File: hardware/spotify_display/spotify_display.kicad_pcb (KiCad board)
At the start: 2 copper layers, 5 parts, among them SW1 SW_Push, SW2 SW_Push, SW3 SW_Push, U1 WEMOS_C3_mini, U2 ST7735

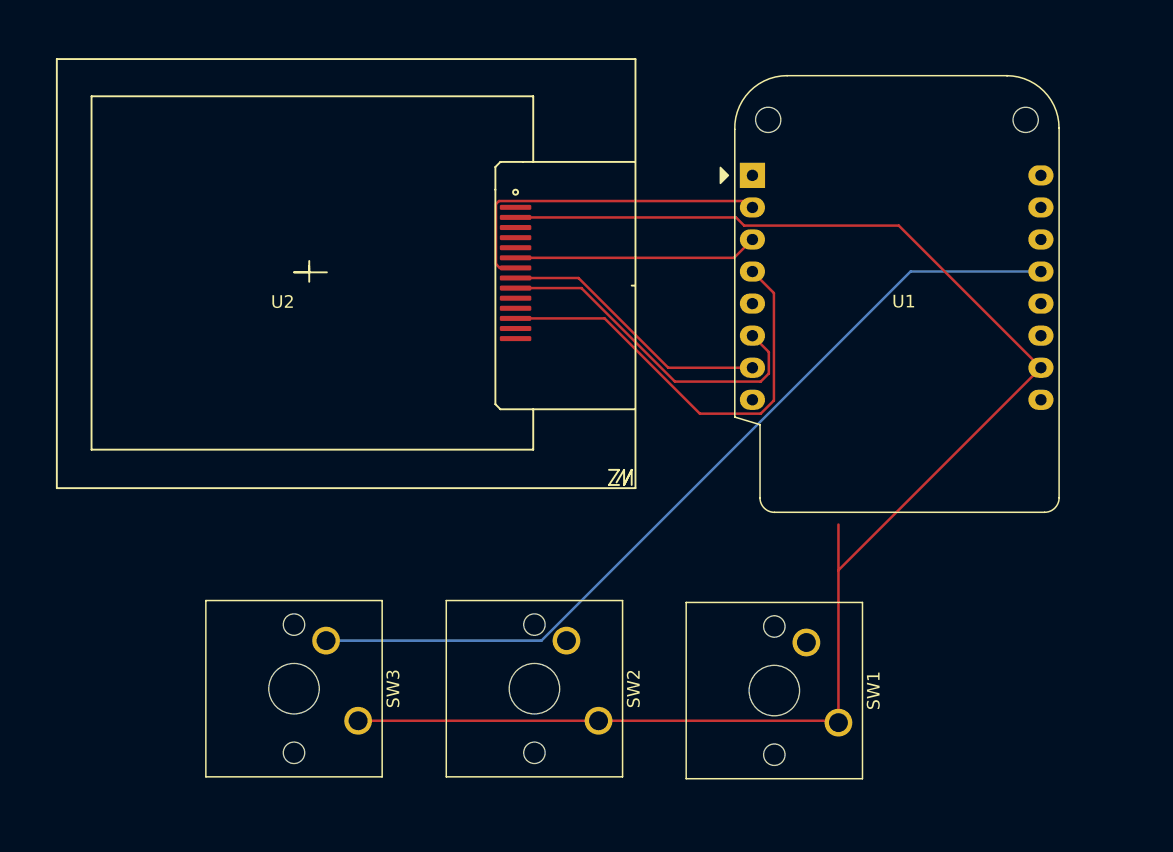
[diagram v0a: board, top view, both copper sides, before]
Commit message: Add Rotary Encoder component and update project files
- Added a new Rotary Encoder symbol to the schematic with properties including reference, value, footprint, and description.
- Updated the KiCad project configuration to specify the plot output directory.
- Adjusted column widths in the project settings for better layout.
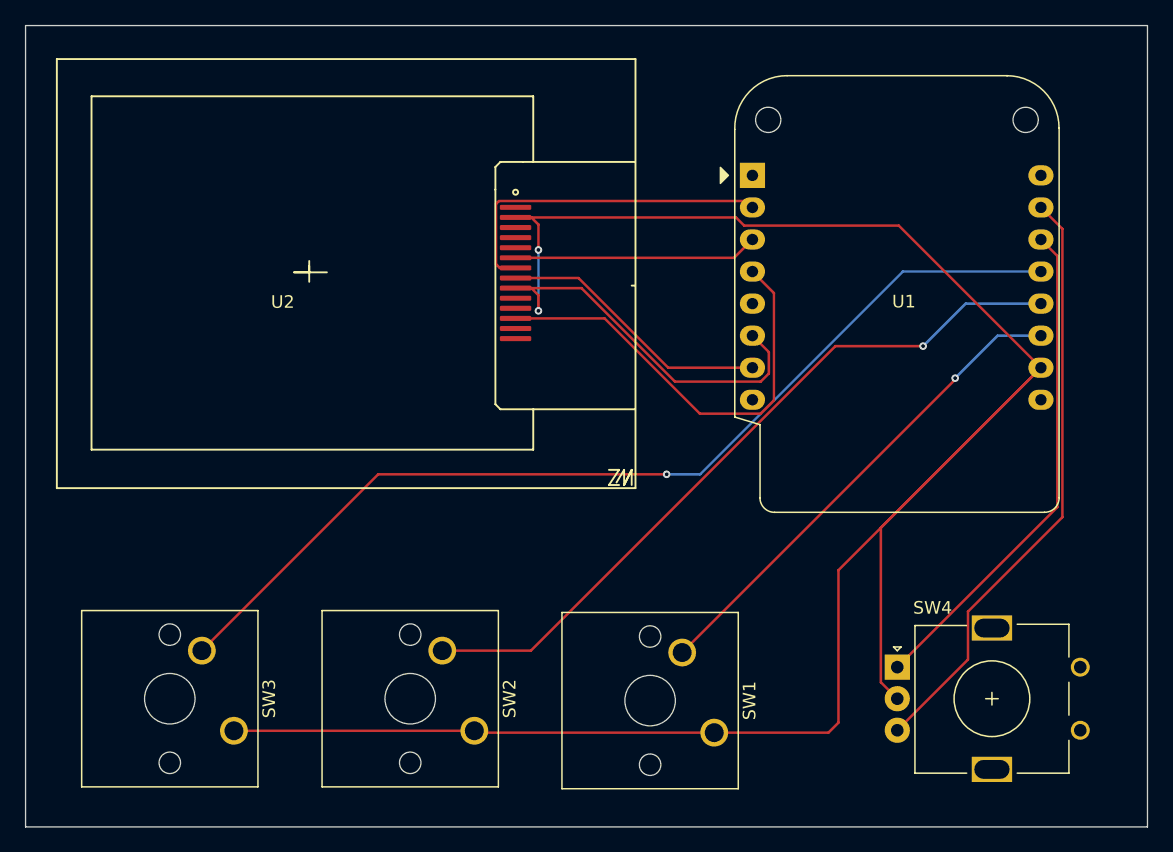
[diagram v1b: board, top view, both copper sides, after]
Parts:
- added SW4: RotaryEncoder, Rotary_Encoder:RotaryEncoder_Alps_EC11E_Vertical_H20mm, F.Cu at (185.9, 91.5)
- moved SW1 9.87 mm to (171.4, 96.7)
- moved SW2 9.87 mm to (152.4, 96.5)
- moved SW3 9.87 mm to (133.3, 96.5)
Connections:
- SW1 pad 1: Net-(U1-GND) -> Net-(U1-D4)
- SW2 pad 1: Net-(U1-GND) -> Net-(U1-D4)
- SW3 pad 1: Net-(U1-GND) -> Net-(U1-D4)
- U1 pad 10: Net-(U1-GND) -> Net-(U1-D4)
- U1 pad 14: unconnected-(U1-D10-Pad14) -> Net-(U1-D10)
- U1 pad 15: unconnected-(U1-RX-Pad15) -> Net-(U1-RX)
- U2 pad 2: Net-(U1-GND) -> Net-(U1-D4)
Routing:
- net Net-(U1-D4): track 26.9 -> 200.7 mm, vias 0 -> 2
- net Net-(U1-GND): track 123.1 -> 0.00 mm
- net Net-(U1-D7): track 0.00 -> 58.8 mm, vias 0 -> 1
- net Net-(U1-RX): track 0.00 -> 47.6 mm
- net Net-(U1-D10): track 0.00 -> 39.7 mm
- net Net-(U1-D6): track 0.00 -> 38.9 mm, vias 0 -> 1
- net Net-(U1-D8): track 68.8 -> 78.9 mm, vias 0 -> 1
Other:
- board outline added: 88.9 x 63.5 mm
